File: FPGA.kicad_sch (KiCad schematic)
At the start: 44 parts, among them IC5 AD817ARZ, IC8 MT25QL128ABA1ESE-0SIT, J13 Conn_02x06_Top_Bottom, J3 Conn_01x02, J4 Conn_02x02_Top_Bottom, J5 Conn_01x02, J8 Conn_02x06_Top_Bottom, U4 ICE5LP1K-SG48, U9 LTC2451xDDB

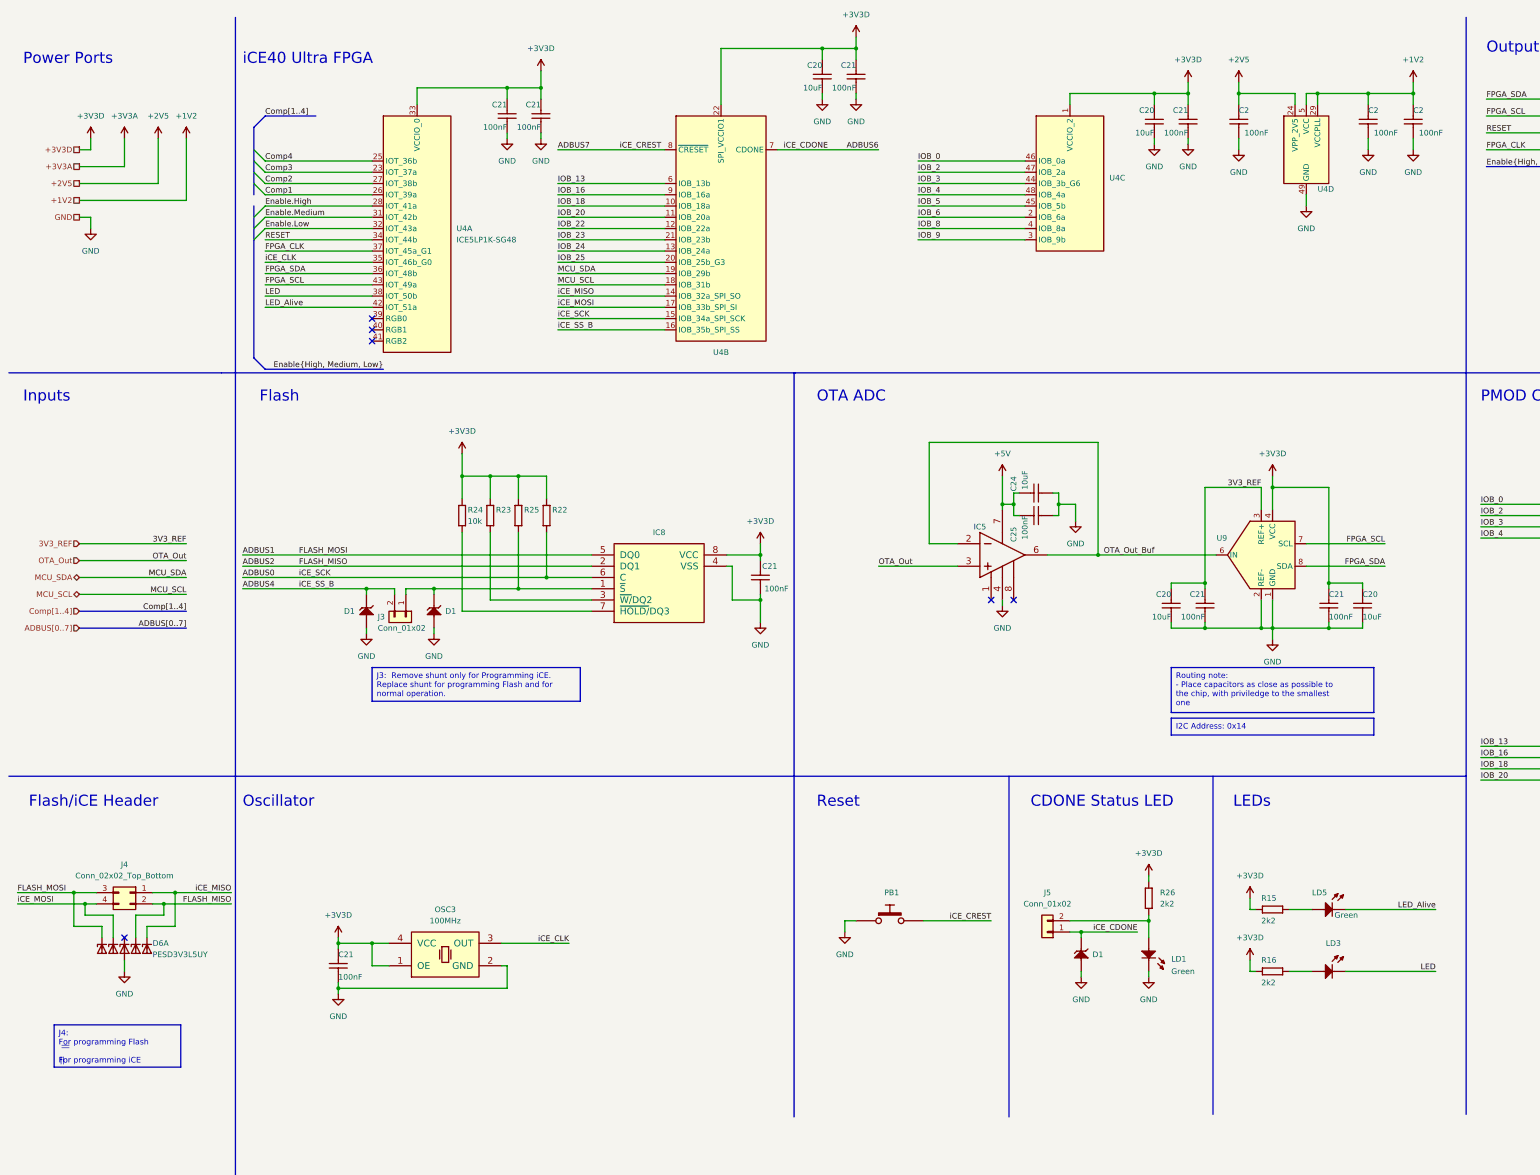
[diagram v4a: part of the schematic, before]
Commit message: Added triax connector, added test points, fixed some mistakes
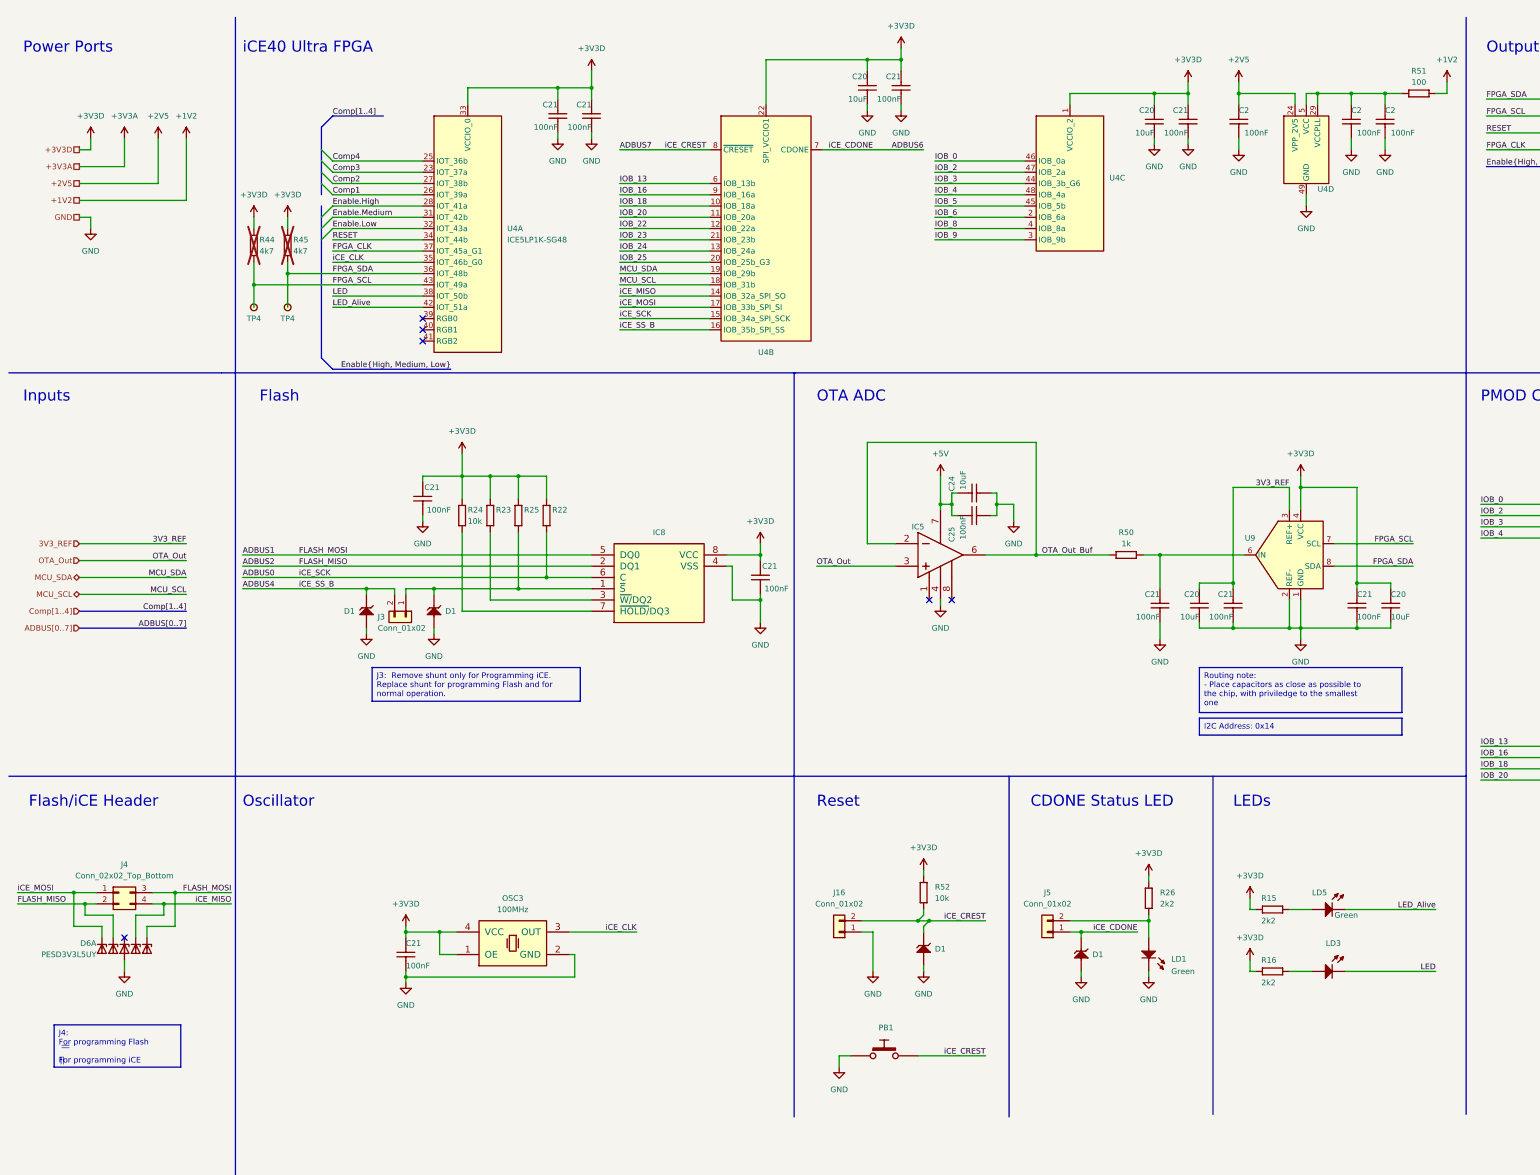
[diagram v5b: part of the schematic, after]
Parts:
- added C21 (x2): CC0603_100NF_50V_10%_X7R, Capacitors SMD:CAPC1608X87N, symbol Capacitors SMD:CC0603_100NF_50V_10%_X7R
- added D1: SMBJ3V3, ICs And Semiconductors SMD:DIOM5436X244N, symbol Diodes:SMBJ3V3
- added J16: Conn_01x02, Connector_PinHeader_2.54mm:PinHeader_1x02_P2.54mm_Vertical, symbol Connector_Generic:Conn_01x02
- added R44, R45: R0603_4K7_1%_0.1W_100PPM, Resistors SMD:RESC1608X55N, symbol Resistors SMD:R0603_4K7_1%_0.1W_100PPM
- added R50: R0603_1K_0.1%_0.1W_25PPM, Resistors SMD:RESC1608X64N, symbol Resistors SMD:R0603_1K_0.1%_0.1W_25PPM
- added R51: R0603_100R_1%_0.1W_100PPM, Resistors SMD:RESC1608X55N, symbol Resistors SMD:R0603_100R_1%_0.1W_100PPM
- added R52: R0603_10K_1%_0.1W_100PPM, Resistors SMD:RESC1608X55N, symbol Resistors SMD:R0603_10K_1%_0.1W_100PPM
- added TP4 (x2): SMD_PAD_1.27X1.27MM, Pads:TPS127, symbol Pads:SMD_PAD_1.27X1.27MM
- J13, J8: footprint (none) -> Connector_PinSocket_2.54mm:PinSocket_2x06_P2.54mm_Vertical
- J3, J5: footprint (none) -> Connector_PinHeader_2.54mm:PinHeader_1x02_P2.54mm_Vertical
- J4: footprint (none) -> Connector_PinHeader_2.54mm:PinHeader_2x02_P2.54mm_Vertical
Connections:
- net +1V2: now also R51.2; no longer C2.1, C2.1, U4.29 (VCCPLL), U4.30 (VCC), U4.5 (VCC)
- net +3V3D: now also C21.1, R44.2, R45.2, R52.1
- net ADBUS7: now also D1.1 (C), J16.2 (Pin_2), R52.2
- net FPGA_SCL: now also R44.1, TP4.1
- net FPGA_SDA: now also R45.1, TP4.1
- net GND: now also C21.2, C21.2, D1.2 (A), J16.1 (Pin_1)
- net OTA_Out_Buf: now also R50.1; no longer U9.6 (IN)
- net iCE_MISO: now also D6.3 (K2), J4.4 (Pin_4); no longer D6.5 (K4), J4.1 (Pin_1)
- net iCE_MOSI: now also D6.5 (K4), J4.1 (Pin_1); no longer D6.3 (K2), J4.4 (Pin_4)
- new net: C21.1, R50.2, U9.6 (IN)
- new net: C2.1, C2.1, R51.1, U4.29 (VCCPLL), U4.30 (VCC), U4.5 (VCC)
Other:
- company: (none) -> CERN
- title: (none) -> ACCURATE 2 Evaluation Board
- moved on the sheet: C2, C20, C21, C24, C25, D6A, IC5, OSC3, PB1, U4A, U4B, U9

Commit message: Polished the schematic a bit
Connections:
- net LED_Alive renamed FPGA_Alive
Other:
- moved on the sheet: C21, D1, J16, LD3, PB1, R16, R22, R23, R24, R25, R52

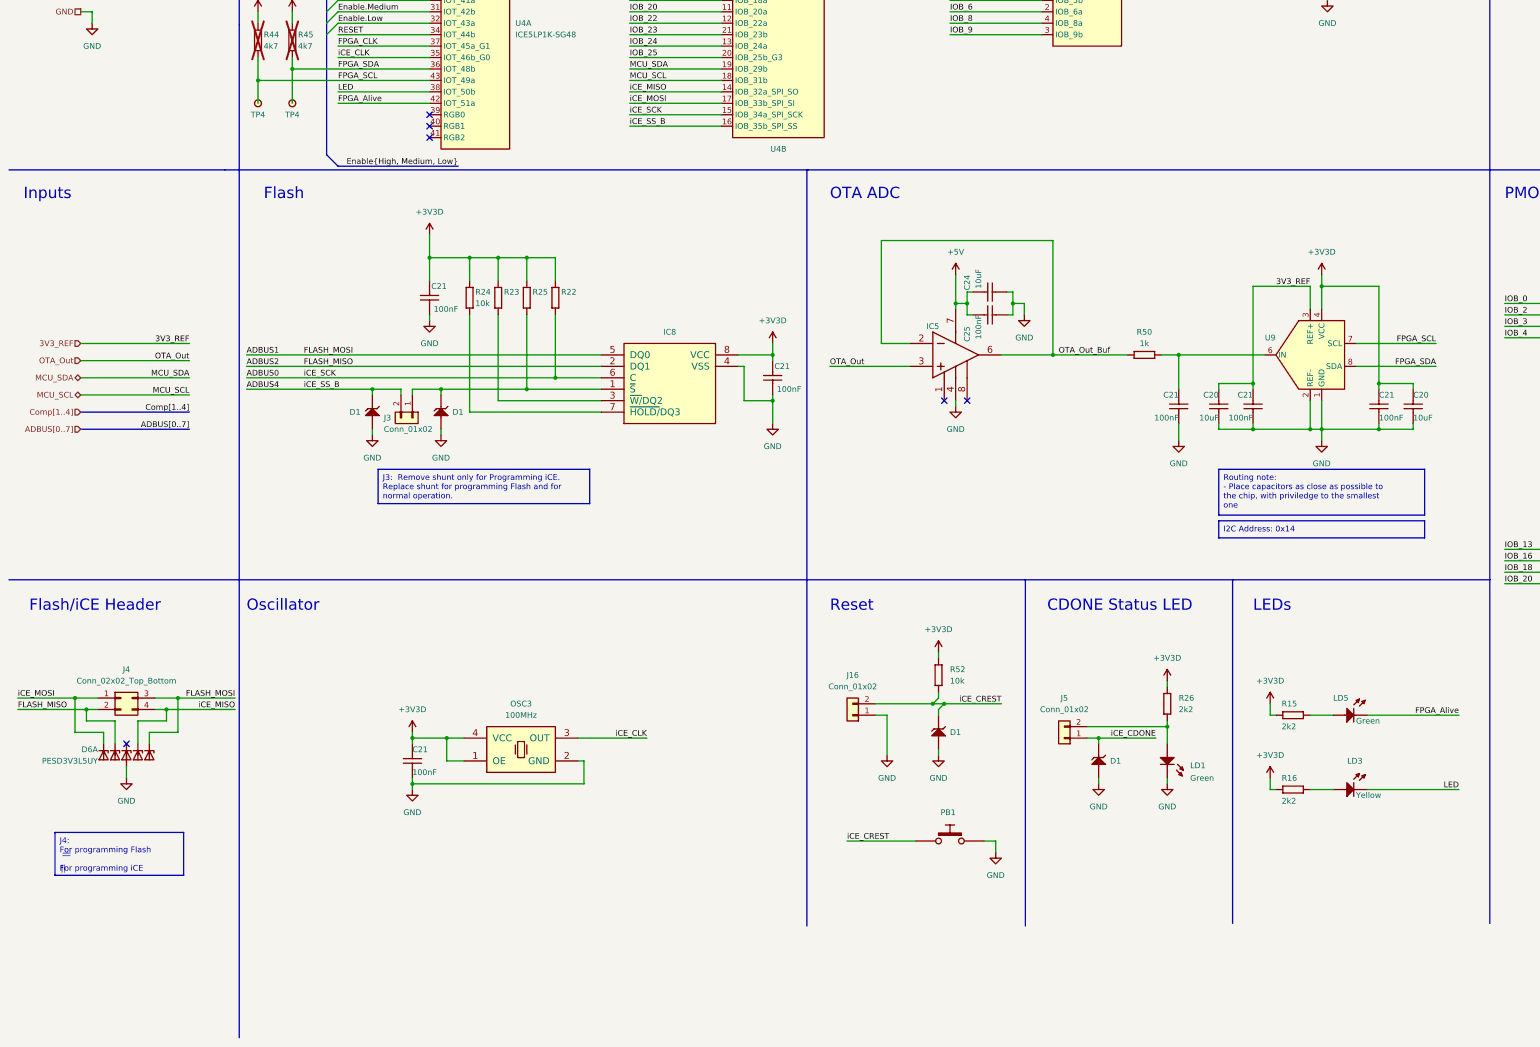
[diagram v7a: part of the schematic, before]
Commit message: Added FPGA prog connector, FPGA UART to USB2Serial IC, RGB LED, fixed mismatch between header symbol and footprint, added more notes, added jumpers
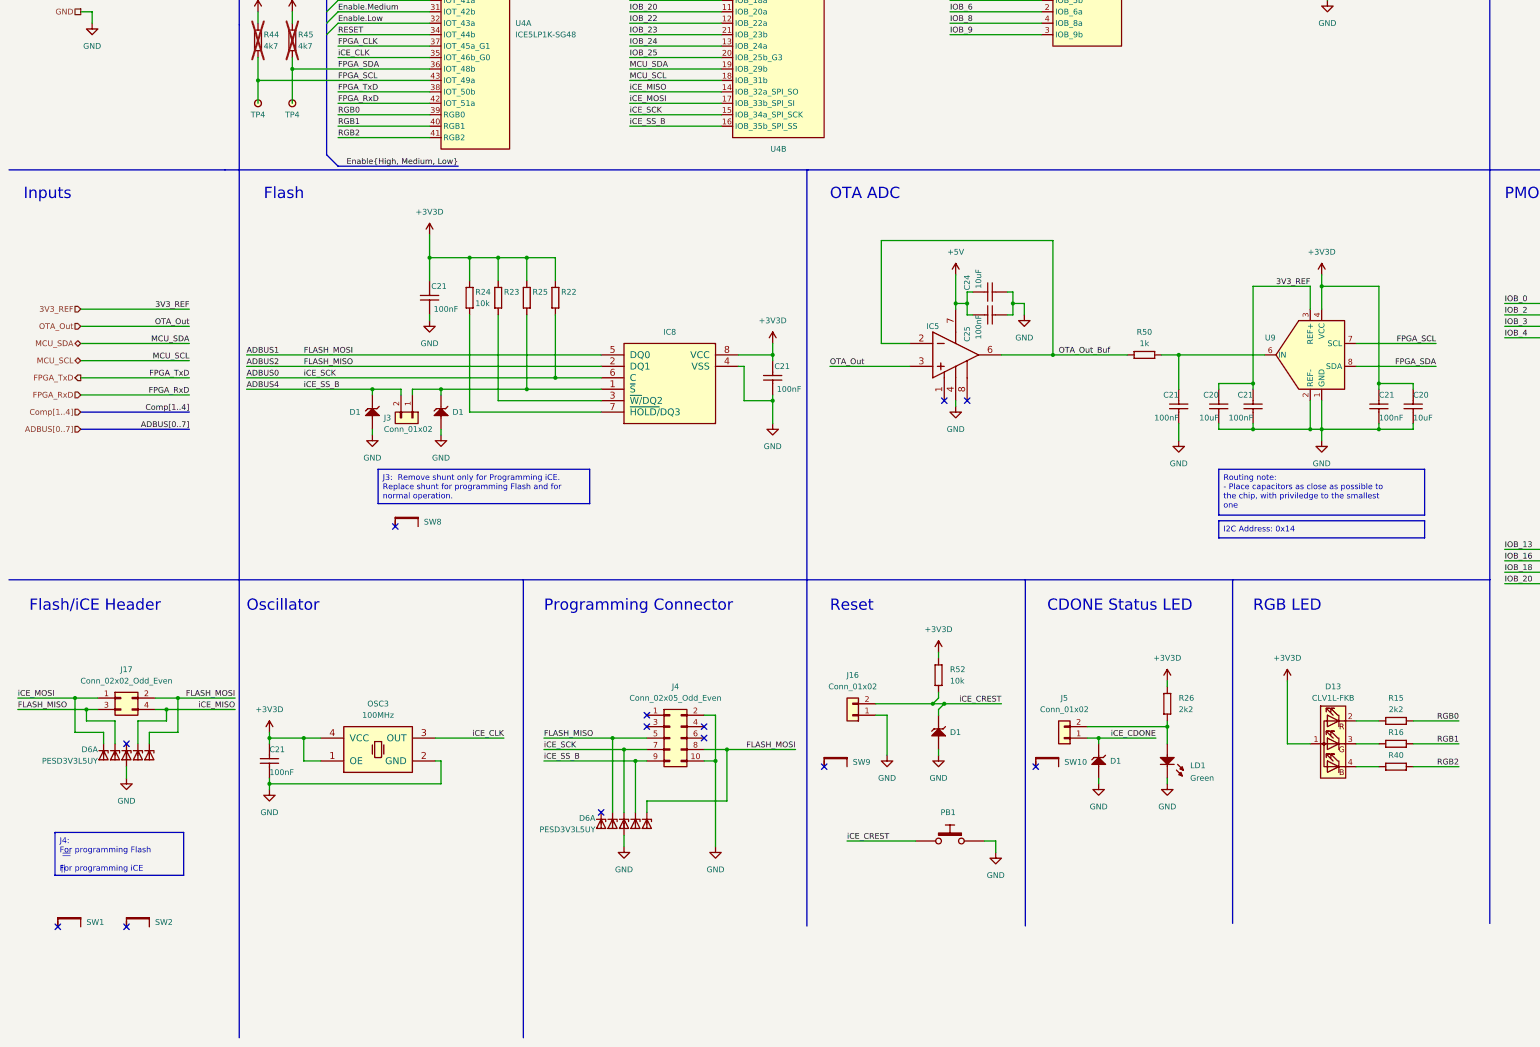
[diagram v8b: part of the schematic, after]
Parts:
- removed J4: Conn_02x02_Top_Bottom, Connector_PinHeader_2.54mm:PinHeader_2x02_P2.54mm_Vertical, symbol Connector_Generic:Conn_02x02_Top_Bottom
- removed LD3: LED_LITEON_LTST-C193KSKT-5A, ICs And Semiconductors SMD:LED_LITEON_LTST-C193KSKT-5A, symbol LEDs & Displays:LED_LITEON_LTST-C193KSKT-5A
- removed LD5: LED_LITEON_LTST-C193KGKT-5A, ICs And Semiconductors SMD:LED_LITEON_LTST-C193KGKT-5A, symbol LEDs & Displays:LED_LITEON_LTST-C193KGKT-5A
- added D13: CLV1L-FKB, LED_SMD:LED_Cree-PLCC4_3.2x2.8mm_CCW, symbol LED:CLV1L-FKB
- added D6: PESD3V3L5UY, Package_TO_SOT_SMD:SOT-363_SC-70-6, symbol Power_Protection:PESD3V3L5UY
- added J17: Conn_02x02_Odd_Even, Connector_PinHeader_2.54mm:PinHeader_2x02_P2.54mm_Vertical, symbol Connector_Generic:Conn_02x02_Odd_Even
- added J4: Conn_02x05_Odd_Even, Connector_PinHeader_2.54mm:PinHeader_2x05_P2.54mm_Vertical, symbol Connector_Generic:Conn_02x05_Odd_Even
- added R40: R0603_2K2_1%_0.1W_100PPM, Resistors SMD:RESC1608X55N, symbol Resistors SMD:R0603_2K2_1%_0.1W_100PPM
- added SW1, SW10, SW2, SW8, SW9: HARWIN_M50-1900005, symbol HARWIN:HARWIN_M50-1900005
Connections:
- net +3V3D: now also D13.1 (A); no longer R15.2, R16.2
- net ADBUS0: now also D6.1 (K1), J4.7 (Pin_7)
- net ADBUS1: now also D6.4 (K3), J17.2 (Pin_2), J4.8 (Pin_8)
- net ADBUS2: now also D6.6 (K5), J17.3 (Pin_3), J4.5 (Pin_5)
- net ADBUS4: now also D6.3 (K2), J4.9 (Pin_9)
- net GND: now also D6.2 (A), J4.10 (Pin_10), J4.2 (Pin_2)
- net iCE_MISO: now also J17.4 (Pin_4)
- net iCE_MOSI: now also J17.1 (Pin_1)
- net RGB0: now reaches R15.1
- net RGB0: now also U4.39 (RGB0)
- net RGB1: now reaches R16.1
- net RGB1: now also U4.40 (RGB1)
- net RGB2: now reaches U4.41 (RGB2)
- net RGB2: now also R40.1
- net FPGA_Alive renamed FPGA_RxD
- net LED renamed FPGA_TxD
- new net: D13.2 (RK), R15.2
- new net: D13.3 (GK), R16.2
- new net: D13.4 (BK), R40.2
- no-connect marks 6 -> 13
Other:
- note added: "Programming Connector"
- note added: "RGB LED"
- note removed: "LEDs"
- moved on the sheet: C21, OSC3
